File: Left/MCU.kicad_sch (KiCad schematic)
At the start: 35 parts, among them U29 Button, U30 nRF52840_aQFN73, X1 32.768 kHz, X2 32MHZ

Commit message: Finished left hand
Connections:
- net P0.05 renamed P1.05
- no-connect marks 2 -> 3

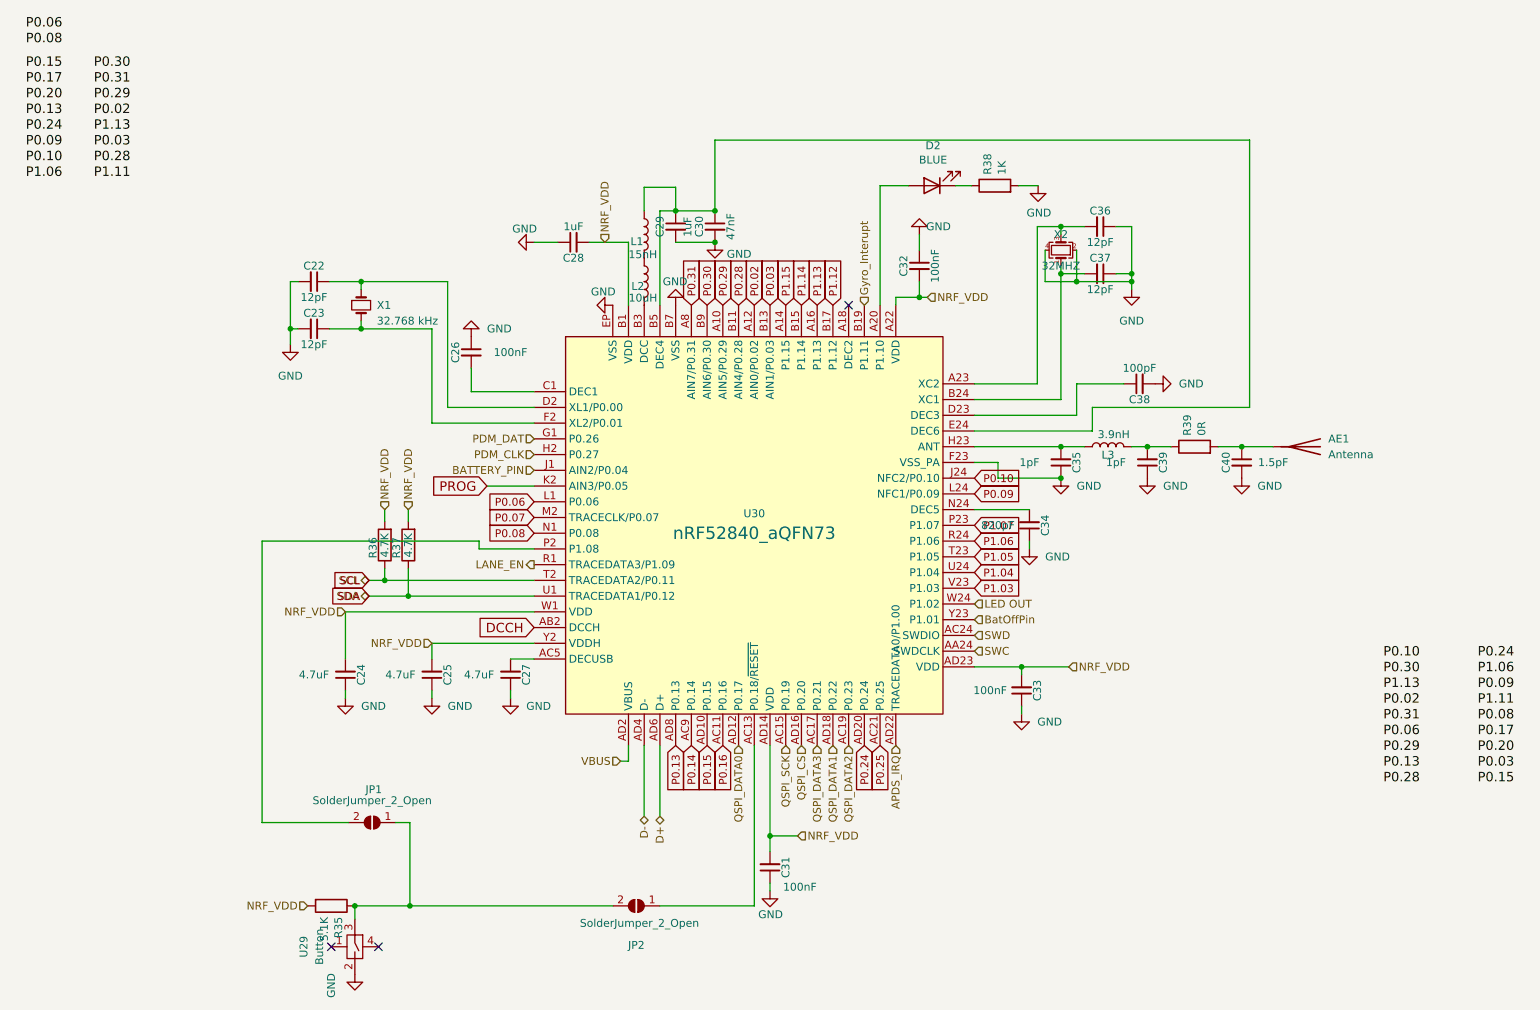
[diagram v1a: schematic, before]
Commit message: upgraded files to kicad7
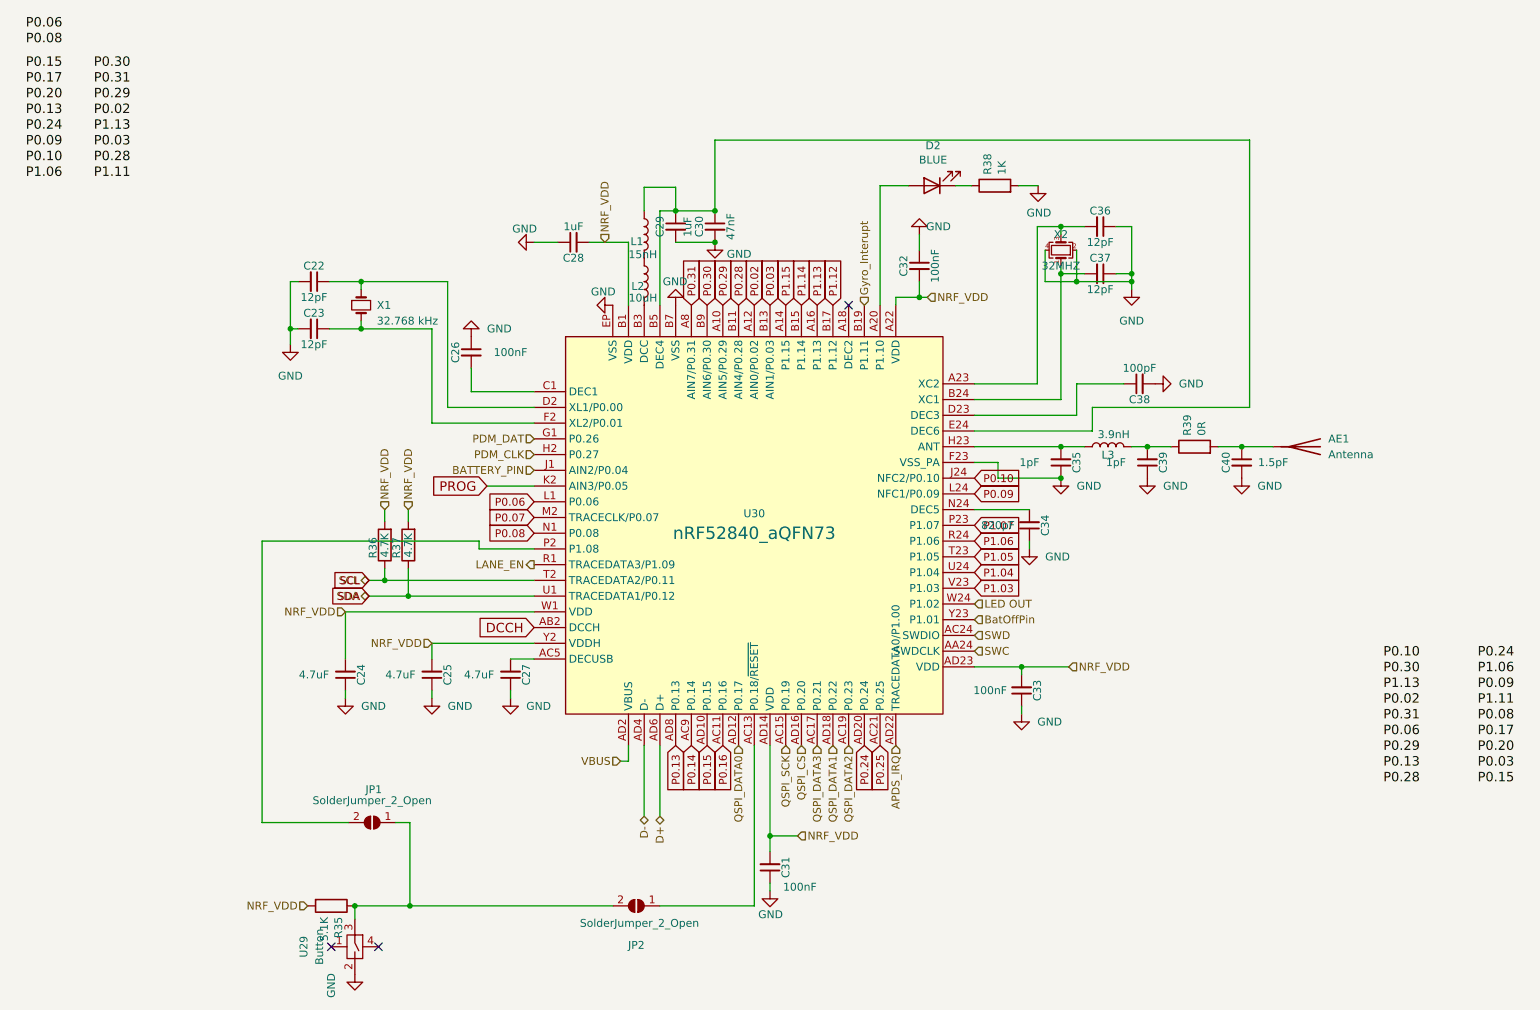
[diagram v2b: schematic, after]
